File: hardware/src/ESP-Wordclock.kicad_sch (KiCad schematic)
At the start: 0 parts

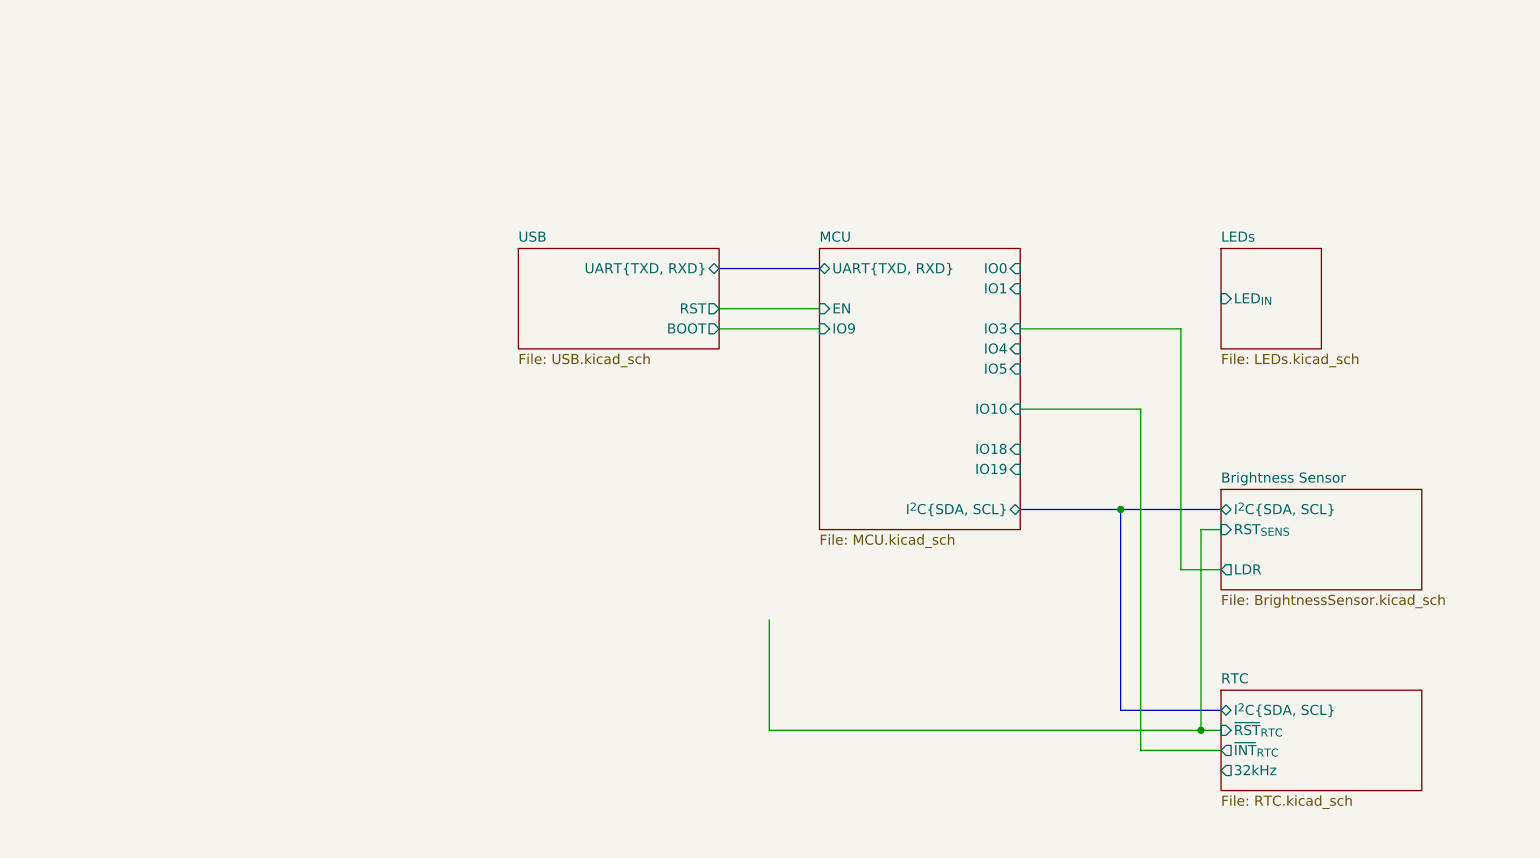
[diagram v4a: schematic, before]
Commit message: Mod: RTC GPIOs
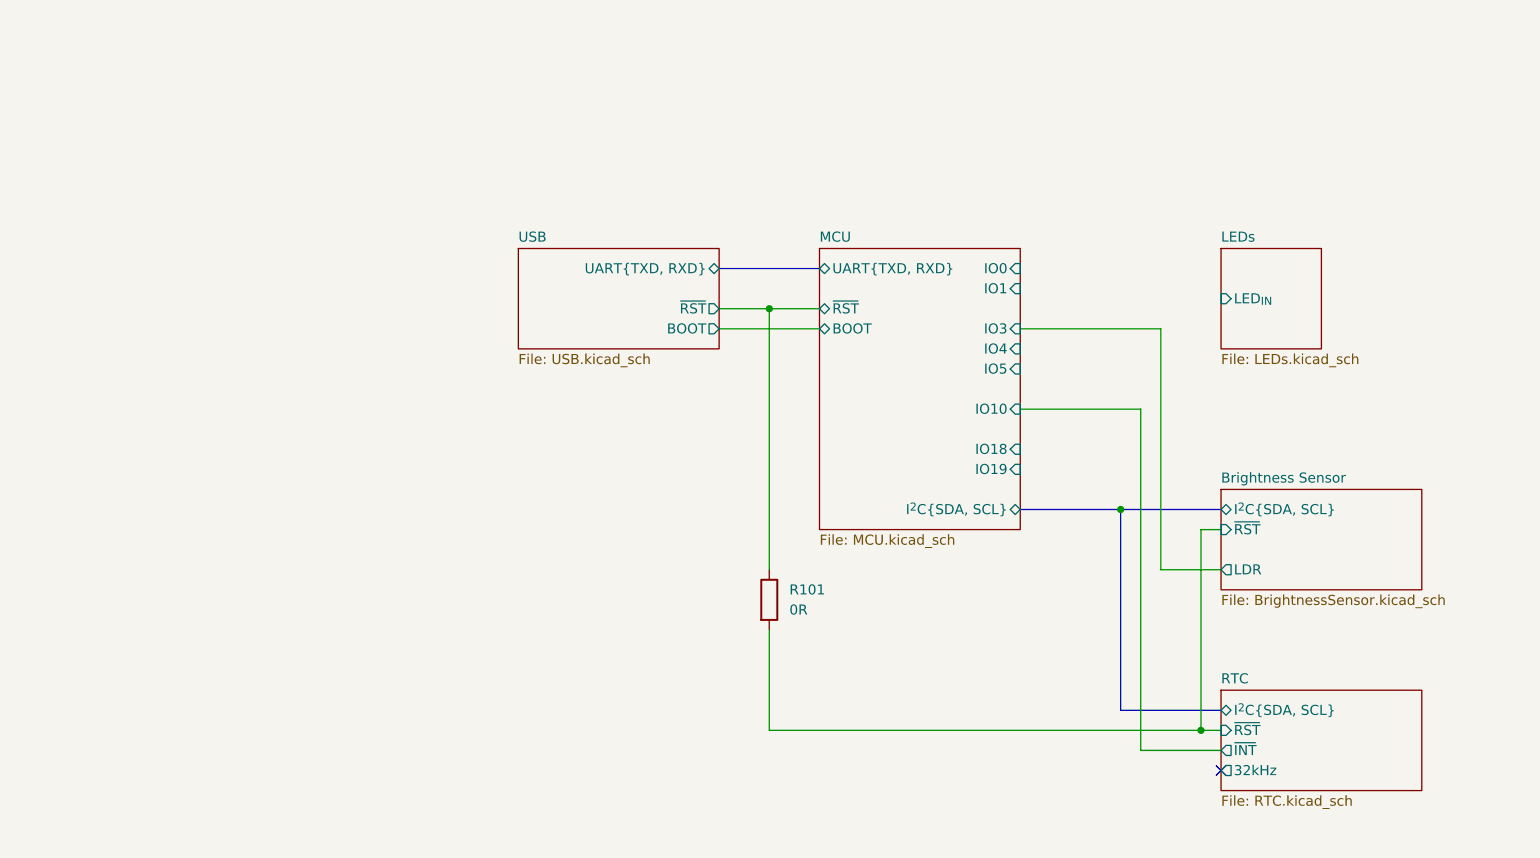
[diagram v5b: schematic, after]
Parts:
- added R101: 0R, symbol Device:R
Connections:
- new net Brightness Sensor/~{RST}: R101.2
- new net MCU/~{RST}: R101.1
- no-connect marks 0 -> 1
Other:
- sheet Brightness Sensor ports: added ~{RST}; removed RST_{SENS}
- sheet MCU ports: added BOOT, ~{RST}; removed EN, IO9
- sheet RTC ports: added ~{INT}, ~{RST}; removed ~{INT}_{RTC}, ~{RST}_{RTC}
- sheet USB ports: added ~{RST}; removed RST
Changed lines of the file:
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@@
 	(title_block
 		(title "Wordclock - Top")
-		(date "2024-10-19")
+		(date "2024-10-20")
 		(rev "A")
 		(company "ElektroNik Zoller")
@@
 	)
 	(junction
+		(at 120.65 71.12)
+		(diameter 0)
+		(color 0 0 0 0)
+	)
+	(junction
 		(at 175.26 124.46)
 		(diameter 0)
 		(color 0 0 0 0)
 	)
-	(wire
-		(pts
-			(xy 120.65 110.49) (xy 120.65 124.46)
+	(no_connect
+		(at 177.8 129.54)
+	)
+	(wire
+		(pts
+			(xy 120.65 71.12) (xy 120.65 104.14)
 		)
 		(stroke
@@
 	(wire
 		(pts
-			(xy 172.72 73.66) (xy 172.72 104.14)
+			(xy 170.18 73.66) (xy 170.18 104.14)
 		)
 		(stroke
@@
 	(wire
 		(pts
-			(xy 152.4 73.66) (xy 172.72 73.66)
+			(xy 152.4 73.66) (xy 170.18 73.66)
 		)
 		(stroke
@@
 	(wire
 		(pts
-			(xy 172.72 104.14) (xy 177.8 104.14)
+			(xy 170.18 104.14) (xy 177.8 104.14)
 		)
 		(stroke
@@
 	(wire
 		(pts
-			(xy 114.3 71.12) (xy 127 71.12)
+			(xy 114.3 71.12) (xy 120.65 71.12)
 		)
 		(stroke
@@
 			(width 0)
 			(type default)
+		)
+	)
+	(wire
+		(pts
+			(xy 120.65 71.12) (xy 127 71.12)
+		)
+		(stroke
+			(width 0)
+			(type default)
+		)
+	)
+	(wire
+		(pts
+			(xy 120.65 111.76) (xy 120.65 124.46)
+		)
+		(stroke
+			(width 0)
+			(type default)
+		)
+	)
+	(symbol
+		(lib_id "Device:R")
+		(at 120.65 107.95 0)
+		(unit 1)
+		(exclude_from_sim no)
+		(in_bom yes)
+		(on_board yes)
+		(dnp no)
+		(fields_autoplaced yes)
+		(property "Reference" "R101"
+			(at 123.19 106.6799 0)
+			(effects
+				(font
+					(size 1.27 1.27)
+				)
+				(justify left)
+			)
+		)
+		(property "Value" "0R"
+			(at 123.19 109.2199 0)
+			(effects
+				(font
+					(size 1.27 1.27)
+				)
+				(justify left)
+			)
+		)
+		(property "Footprint" ""
+			(at 118.872 107.95 90)
+			(effects
+				(font
+					(size 1.27 1.27)
+				)
+				(hide yes)
+			)
+		)
+		(property "Datasheet" "~"
+			(at 120.65 107.95 0)
+			(effects
+				(font
+					(size 1.27 1.27)
+				)
+				(hide yes)
+			)
+		)
+		(property "Description" "Resistor"
+			(at 120.65 107.95 0)
+			(effects
+				(font
+					(size 1.27 1.27)
+				)
+				(hide yes)
+			)
+		)
+		(pin "2"
+		)
+		(pin "1"
+		)
+		(instances
+			(project ""
+				(path "/bfaac094-0365-40a4-8b7a-d4d62ace544e"
+					(reference "R101")
+					(unit 1)
+				)
+			)
 		)
 	)
@@
 			)
 		)
-		(pin "IO9" input
-			(at 127 73.66 180)
-			(effects
-				(font
-					(size 1.27 1.27)
-				)
-				(justify left)
-			)
-		)
 		(pin "IO19" input
 			(at 152.4 91.44 0)
@@
 			)
 		)
-		(pin "EN" input
-			(at 127 71.12 180)
-			(effects
-				(font
-					(size 1.27 1.27)
-				)
-				(justify left)
-			)
-		)
 		(pin "IO1" input
 			(at 152.4 68.58 0)
@@
 				)
 				(justify right)
+			)
+		)
+		(pin "BOOT" bidirectional
+			(at 127 73.66 180)
+			(effects
+				(font
+					(size 1.27 1.27)
+				)
+				(justify left)
+			)
+		)
+		(pin "~{RST}" bidirectional
+			(at 127 71.12 180)
+			(effects
+				(font
+					(size 1.27 1.27)
+				)
+				(justify left)
 			)
 		)
@@
 			)
 		)
-		(pin "RST" output
+		(pin "~{RST}" output
 			(at 114.3 71.12 0)
 			(effects
@@
 			)
 		)
-		(pin "~{INT}_{RTC}" output
-			(at 177.8 127 180)
-			(effects
-				(font
-					(size 1.27 1.27)
-				)
-				(justify left)
-			)
-		)
 		(pin "32kHz" output
 			(at 177.8 129.54 180)
@@
 			)
 		)
-		(pin "~{RST}_{RTC}" input
+		(pin "~{INT}" output
+			(at 177.8 127 180)
+			(effects
+				(font
+					(size 1.27 1.27)
+				)
+				(justify left)
+			)
+		)
+		(pin "~{RST}" input
 			(at 177.8 124.46 180)
 			(effects
@@
 			)
 		)
-		(pin "RST_{SENS}" input
+		(pin "~{RST}" input
 			(at 177.8 99.06 180)
 			(effects

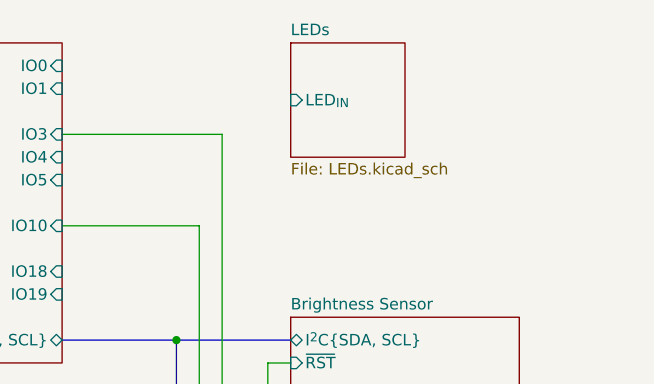
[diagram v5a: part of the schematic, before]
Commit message: Add: Level Shifter +3V3 to +5V
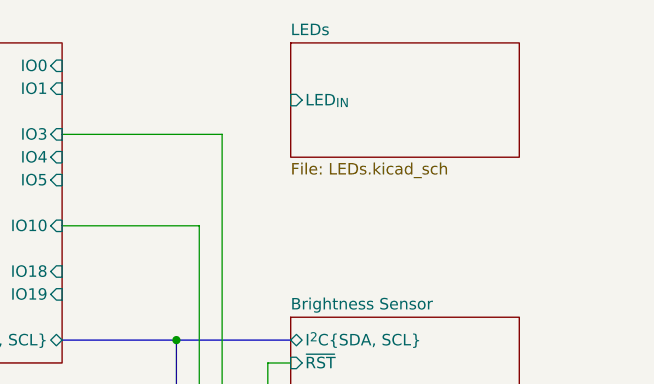
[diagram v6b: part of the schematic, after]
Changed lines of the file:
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@@
 	(sheet
 		(at 177.8 63.5)
-		(size 12.7 12.7)
+		(size 25.4 12.7)
 		(fields_autoplaced yes)
 		(stroke

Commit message: Mod: Changed date and made some small corrections
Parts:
- removed R101: 0R, symbol Device:R
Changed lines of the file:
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@@
 	(title_block
 		(title "Wordclock - Top")
-		(date "2024-10-20")
+		(date "2024-10-21")
 		(rev "A")
 		(company "ElektroNik Zoller")
@@
 	)
 	(junction
-		(at 120.65 71.12)
-		(diameter 0)
-		(color 0 0 0 0)
-	)
-	(junction
 		(at 175.26 124.46)
 		(diameter 0)
@@
 	(no_connect
 		(at 177.8 129.54)
-	)
-	(wire
-		(pts
-			(xy 120.65 71.12) (xy 120.65 104.14)
-		)
-		(stroke
-			(width 0)
-			(type default)
-		)
 	)
 	(wire
@@
 	(wire
 		(pts
-			(xy 114.3 71.12) (xy 120.65 71.12)
-		)
-		(stroke
-			(width 0)
-			(type default)
-		)
-	)
-	(wire
-		(pts
 			(xy 177.8 99.06) (xy 175.26 99.06)
 		)
@@
 	(wire
 		(pts
-			(xy 120.65 71.12) (xy 127 71.12)
+			(xy 114.3 71.12) (xy 127 71.12)
 		)
 		(stroke
@@
 		)
 	)
-	(wire
-		(pts
-			(xy 120.65 111.76) (xy 120.65 124.46)
-		)
-		(stroke
-			(width 0)
-			(type default)
-		)
-	)
-	(symbol
-		(lib_id "Device:R")
-		(at 120.65 107.95 0)
-		(unit 1)
-		(exclude_from_sim no)
-		(in_bom yes)
-		(on_board yes)
-		(dnp no)
-		(fields_autoplaced yes)
-		(property "Reference" "R101"
-			(at 123.19 106.6799 0)
-			(effects
-				(font
-					(size 1.27 1.27)
-				)
-				(justify left)
-			)
-		)
-		(property "Value" "0R"
-			(at 123.19 109.2199 0)
-			(effects
-				(font
-					(size 1.27 1.27)
-				)
-				(justify left)
-			)
-		)
-		(property "Footprint" ""
-			(at 118.872 107.95 90)
-			(effects
-				(font
-					(size 1.27 1.27)
-				)
-				(hide yes)
-			)
-		)
-		(property "Datasheet" "~"
-			(at 120.65 107.95 0)
-			(effects
-				(font
-					(size 1.27 1.27)
-				)
-				(hide yes)
-			)
-		)
-		(property "Description" "Resistor"
-			(at 120.65 107.95 0)
-			(effects
-				(font
-					(size 1.27 1.27)
-				)
-				(hide yes)
-			)
-		)
-		(pin "2"
-		)
-		(pin "1"
-		)
-		(instances
-			(project ""
-				(path "/bfaac094-0365-40a4-8b7a-d4d62ace544e"
-					(reference "R101")
-					(unit 1)
-				)
-			)
-		)
-	)

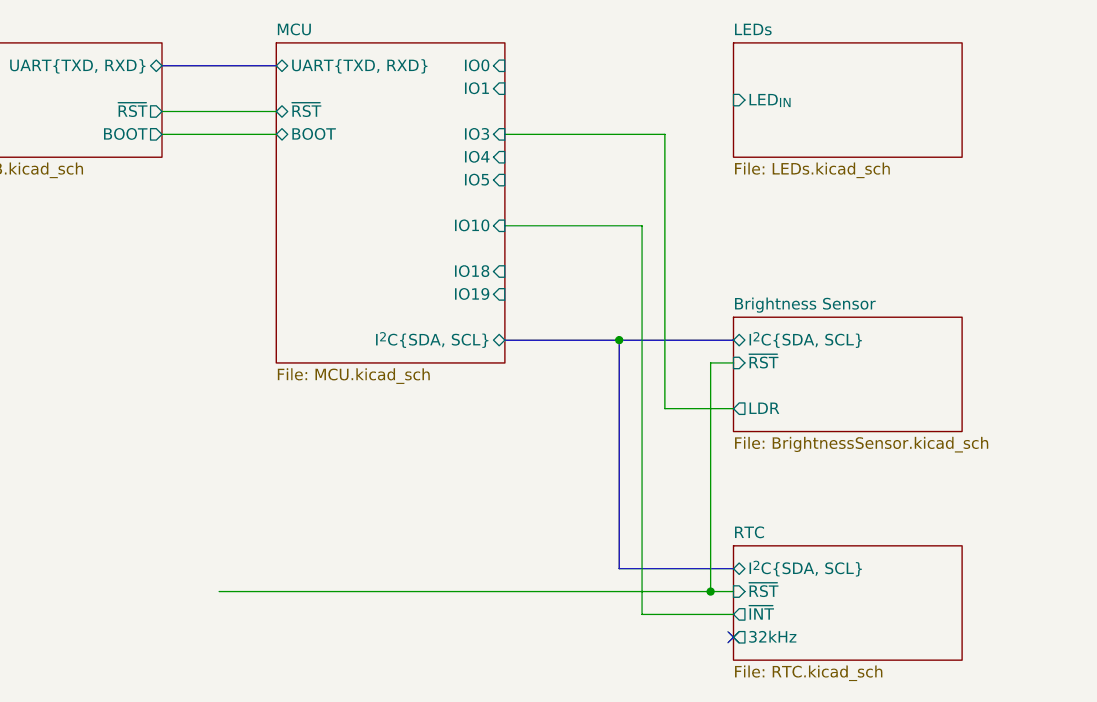
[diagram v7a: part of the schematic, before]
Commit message: Add: Brightness sensors to the schematic
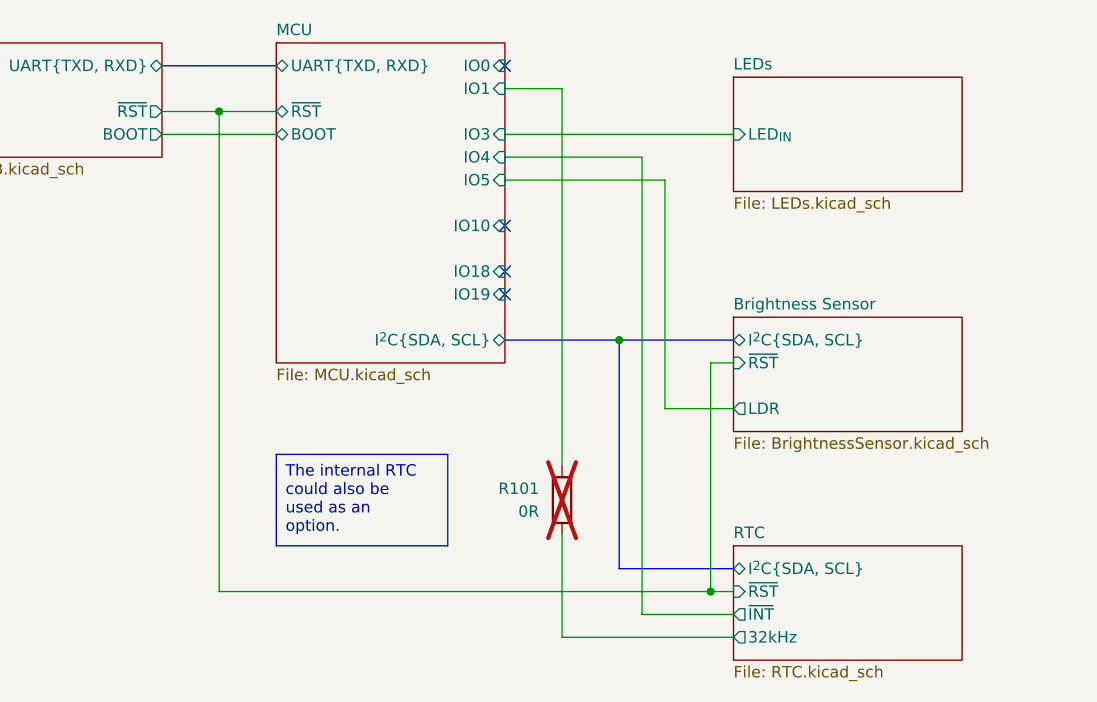
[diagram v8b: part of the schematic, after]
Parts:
- added R101: 0R, symbol Device:R
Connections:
- net MCU/IO1: now also R101.1
- net RTC/32kHz: now also R101.2
- no-connect marks 1 -> 4
